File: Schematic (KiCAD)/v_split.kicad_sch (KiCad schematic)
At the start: 108 parts, among them P1 INVERT, P10 NAND_2, P11 NAND_2, P12,13,18,19,25,26 Reg 3 DFF-Reset, P14 INVERT, P15 T-FF Preload, P16 NAND_2, P17 NAND_2, P2 NOR_2, P20 INVERT, P21 T-FF Preload, P22 BUFFER, P23 NAND_2, P24 NAND_2, P28 BUFFER, P3 INVERT, P6 Reg 2 DFF-Reset N, P8 INVERT, P9 T-FF Preload, T1 INVERT, T10 INVERT, T12 T-FF Preload, T13 INVERT, T14 INVERT, T15 T-FF Preload, T16 INVERT, T17 INVERT, T18 T-FF Preload, T19 INVERT, T2 INVERT, T20 INVERT, T21 T-FF Preload, T22 INVERT, T23 INVERT, T24 T-FF Preload, T25 INVERT, T26 INVERT, T27 T-FF Preload, T28 INVERT, T29 INVERT, T3 NAND_2, T30 T-FF Preload, T31 INVERT, T4 JK-FF Reset, T5 BUFFER, T6 INVERT, T7 INVERT, T8 T-FF Preload, T9 INVERT, X1 INVERT, X2 NAND_2

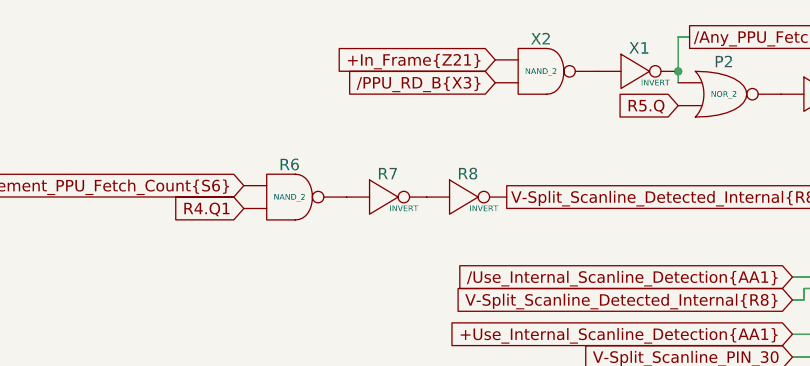
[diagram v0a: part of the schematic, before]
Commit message: - Started work on the pulse channels.  - Solved at least 2 of the red traces in the SVG.  - Finally realized that "Unknown 4to1" cells are actually just ordinary And-Or-Invert "AOI22" cells.
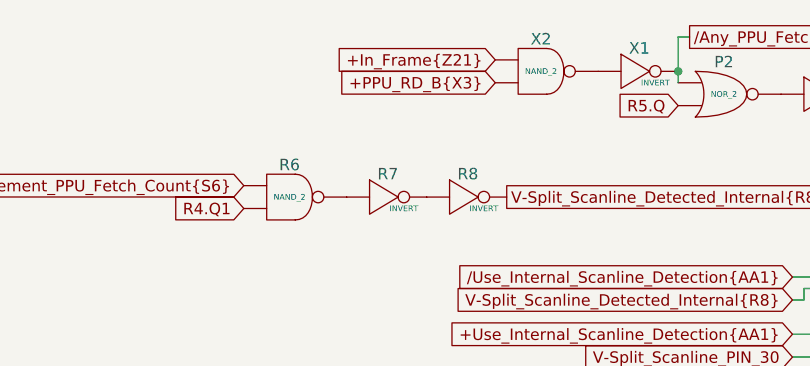
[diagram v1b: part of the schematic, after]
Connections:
- net /PPU_RD_B{X3} is gone; now on net +PPU_RD_B{X3}: X2. (X)
- net at V4. (X): now also V5. (X); no longer V6. (X)
- net at V9. (X): now also V11. (X); no longer V4. (X)
- net at R27. (/Q): now also R26. (X)
- net at R26. (X): now also R29. (X); no longer R27. (/Q)
- net at P9. (/Q): now also P8. (X); no longer P10. (X)
- net at T2. (X): now also T1. (X); no longer T3. (X)
- net at P28. (X): now also R26. (X); no longer P12,13,18,19,25,26. (Q2)
- net at T20. (X): now also T21. (/Q); no longer V27. (X)
- net at T21. (/Q): now also V28. (X), V29. (X); no longer T20. (X)
- net at R7. (X): now also R8. (X); no longer R6. (X)
- net at P21. (/Q): no longer P22. (X)
- net at T14. (X): now also T15. (/Q); no longer V19. (X)
- net at P1. (X): now also P2. (X); no longer S5. (X)
- net at T29. (X): now also V36. (X); no longer T30. (/Q)
- net at P15. (/Q): now also P20. (X), P21. (/Q); no longer P16. (X)
- net at BH28. (X): now also T4. (/Q); no longer BH29. (X)
- net at V11. (X): now also V10. (X); no longer V12. (X)
- net at T26. (X): now also T27. (/Q); no longer V33. (X)
- net at T27. (/Q): no longer T26. (X)
- net at T12. (/Q): now also T8. (/Q), T9. (X)
- net at T10. (X): now also V16. (X); no longer T12. (/Q)
- net at T30. (/Q): now also V37. (X), V38. (X); no longer T31. (X)
- net at T23. (X): now also V30. (X); no longer T24. (/Q)
- net at T15. (/Q): no longer T14. (X)
- net at BH32. (X): now also BH31. (X); no longer T4. (/Q)
- net at T7. (X): now also T8. (/Q); no longer V13. (X)
- net +PPU_RD_B{X3}: now reaches X2. (X)
- net +PPU_RD_B{X3}: no longer X1. (X)
- net at T18. (/Q): now also T17. (X)
- net at T17. (X): now also V22. (X); no longer T18. (/Q)
- new net: N1. (X), P6. (/Q1)
- new net: V4. (X), V6. (X)
- new net: V3. (X), V4. (X)
- new net: V4. (X), V9. (X)
- new net: R27. (/Q), R28. (X)
- new net: R27. (/Q), R29. (X)
- new net: P3. (X), R1. (X)
- new net: P10. (X), P9. (/Q)
- new net: P10. (X), P11. (X), P9. (/Q)
- new net: T2. (X), T3. (X)
- new net: T3. (X), T4. (/Q)
- new net: T18. (/Q), T19. (X), T21. (/Q)
- new net: T15. (/Q), T16. (X), T18. (/Q)
- new net: V6. (X), W2. (Q4)
- new net: P12,13,18,19,25,26. (Q2), P28. (X)
- new net: P12,13,18,19,25,26. (Q2), P17. (X)
- new net: P11. (X), P12,13,18,19,25,26. (Q2)
- new net: P12,13,18,19,25,26. (Q2), P24. (X)
- new net: P14. (X), P15. (/Q), P9. (/Q)
- new net: T20. (X), V27. (X)
- new net: R6. (X), R7. (X)
- new net: T27. (/Q), V34. (X), V35. (X)
- new net: V33. (X), V34. (X)
- new net: P21. (/Q), P22. (X)
- new net: V19. (X), V20. (X)
- new net: T14. (X), V19. (X)
- new net: V7. (X), V8. (/Q)
- new net: P1. (X), S5. (X)
- new net: V27. (X), V28. (X)
- new net: V3. (X), W2. (Q4)
- new net: T29. (X), T30. (/Q)
- new net: P15. (/Q), P16. (X), P17. (X)
- new net: P15. (/Q), P16. (X)
- new net: T18. (/Q), V23. (X), V26. (X)
- new net: V26. (X), W3,V24,V25,V41. (Q7)
- new net: V8. (/Q), V9. (X)
- new net: V35. (X), W3,V24,V25,V41. (Q7)
- new net: BH28. (X), BH29. (X)
- new net: V11. (X), V12. (X)
- new net: V12. (X), W2. (Q4)
- new net: P21. (/Q), P23. (X)
- new net: P21. (/Q), P23. (X), P24. (X)
- new net: T24. (/Q), T25. (X), T27. (/Q)
- new net: T26. (X), V33. (X)
- new net: T15. (/Q), V20. (X), V21. (X)
- new net: R4. (Q1), S4. (X)
- new net: R4. (Q1), S3. (X)
- new net: T12. (/Q), V17. (X), V18. (X)
- new net: T12. (/Q), T13. (X), T15. (/Q)
- new net: T10. (X), T12. (/Q)
- new net: V22. (X), V23. (X)
- new net: V18. (X), W3,V24,V25,V41. (Q7)
- new net: T30. (/Q), T31. (X)
- new net: T23. (X), T24. (/Q)
- new net: T21. (/Q), T22. (X), T24. (/Q)
- new net: BH29. (X), BH30. (X)
- new net: BH32. (X), T4. (/Q)
- new net: T27. (/Q), T28. (X), T30. (/Q)
- new net: V16. (X), V17. (X)
- new net: T7. (X), V13. (X)
- new net: V13. (X), V14. (X)
- new net: V5. (X), W2. (Q4)
- new net: V36. (X), V37. (X)
- new net: T24. (/Q), V31. (X), V32. (X)
- new net: V32. (X), W3,V24,V25,V41. (Q7)
- new net: V29. (X), W3,V24,V25,V41. (Q7)
- new net: X1. (X), X2. (X)
- new net: T6. (X), V11. (X)
- new net: V30. (X), V31. (X)
- new net: V38. (X), W3,V24,V25,V41. (Q7)
- new net: T8. (/Q), V14. (X), V15. (X)
- new net: V2. (X), W2. (Q4)
- new net: V21. (X), W3,V24,V25,V41. (Q7)
- new net: V15. (X), W3,V24,V25,V41. (Q7)
- new net: V10. (X), W2. (Q4)
- now unconnected: P21. (/Q), P21. (/Q), P21. (/Q), T15. (/Q), T15. (/Q), T15. (/Q), T24. (/Q), T24. (/Q), T24. (/Q), T27. (/Q), T27. (/Q), T27. (/Q)
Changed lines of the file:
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@@
 		)
 	)
-	(global_label "{slash}PPU_RD_B{X3}"
+	(global_label "+PPU_RD_B{X3}"
 		(shape input)
 		(at 264.16 24.13 180)
@@
 		)
 		(property "Intersheetrefs" "${INTERSHEET_REFS}"
-			(at 246.1162 24.13 0)
+			(at 245.8743 24.13 0)
 			(effects
 				(font

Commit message: - Pulse DAC logic is now complete.  - The 4-bit adders are verified correct using Excel.    - This revealed 1 tracing error and also 3 XNOR gates that are actually XOR in this case.  - Now including a PDF version of the schematic.
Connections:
- net at V4. (X): now also V5. (X); no longer V6. (X)
- net at V9. (X): now also V11. (X); no longer V4. (X)
- net at R27. (/Q): now also R26. (X)
- net at R26. (X): now also R29. (X); no longer R27. (/Q)
- net at P9. (/Q): now also P8. (X); no longer P10. (X)
- net at T2. (X): now also T1. (X); no longer T3. (X)
- net at P28. (X): now also R26. (X); no longer P12,13,18,19,25,26. (Q2)
- net at T20. (X): now also T21. (/Q); no longer V27. (X)
- net at T21. (/Q): now also V28. (X), V29. (X); no longer T20. (X)
- net at R7. (X): now also R8. (X); no longer R6. (X)
- net at P21. (/Q): no longer P22. (X)
- net at T14. (X): now also T15. (/Q); no longer V19. (X)
- net at P1. (X): now also P2. (X); no longer S5. (X)
- net at T29. (X): now also V36. (X); no longer T30. (/Q)
- net at P15. (/Q): now also P20. (X), P21. (/Q); no longer P16. (X)
- net at BH28. (X): now also T4. (/Q); no longer BH29. (X)
- net at V11. (X): now also V10. (X); no longer V12. (X)
- net at T26. (X): now also T27. (/Q); no longer V33. (X)
- net at T27. (/Q): no longer T26. (X)
- net at T12. (/Q): now also T8. (/Q), T9. (X)
- net at T10. (X): now also V16. (X); no longer T12. (/Q)
- net at T30. (/Q): now also V37. (X), V38. (X); no longer T31. (X)
- net at T23. (X): now also V30. (X); no longer T24. (/Q)
- net at T15. (/Q): no longer T14. (X)
- net at BH32. (X): now also BH31. (X); no longer T4. (/Q)
- net at T7. (X): now also T8. (/Q); no longer V13. (X)
- net at T18. (/Q): now also T17. (X)
- net at T17. (X): now also V22. (X); no longer T18. (/Q)
- new net: N1. (X), P6. (/Q1)
- new net: V4. (X), V6. (X)
- new net: V3. (X), V4. (X)
- new net: V4. (X), V9. (X)
- new net: R27. (/Q), R28. (X)
- new net: R27. (/Q), R29. (X)
- new net: P3. (X), R1. (X)
- new net: P10. (X), P9. (/Q)
- new net: P10. (X), P11. (X), P9. (/Q)
- new net: T2. (X), T3. (X)
- new net: T3. (X), T4. (/Q)
- new net: T18. (/Q), T19. (X), T21. (/Q)
- new net: T15. (/Q), T16. (X), T18. (/Q)
- new net: V6. (X), W2. (Q4)
- new net: P12,13,18,19,25,26. (Q2), P28. (X)
- new net: P12,13,18,19,25,26. (Q2), P17. (X)
- new net: P11. (X), P12,13,18,19,25,26. (Q2)
- new net: P12,13,18,19,25,26. (Q2), P24. (X)
- new net: P14. (X), P15. (/Q), P9. (/Q)
- new net: T20. (X), V27. (X)
- new net: R6. (X), R7. (X)
- new net: T27. (/Q), V34. (X), V35. (X)
- new net: V33. (X), V34. (X)
- new net: P21. (/Q), P22. (X)
- new net: V19. (X), V20. (X)
- new net: T14. (X), V19. (X)
- new net: V7. (X), V8. (/Q)
- new net: P1. (X), S5. (X)
- new net: V27. (X), V28. (X)
- new net: V3. (X), W2. (Q4)
- new net: T29. (X), T30. (/Q)
- new net: P15. (/Q), P16. (X), P17. (X)
- new net: P15. (/Q), P16. (X)
- new net: T18. (/Q), V23. (X), V26. (X)
- new net: V26. (X), W3,V24,V25,V41. (Q7)
- new net: V8. (/Q), V9. (X)
- new net: V35. (X), W3,V24,V25,V41. (Q7)
- new net: BH28. (X), BH29. (X)
- new net: V11. (X), V12. (X)
- new net: V12. (X), W2. (Q4)
- new net: P21. (/Q), P23. (X)
- new net: P21. (/Q), P23. (X), P24. (X)
- new net: T24. (/Q), T25. (X), T27. (/Q)
- new net: T26. (X), V33. (X)
- new net: T15. (/Q), V20. (X), V21. (X)
- new net: R4. (Q1), S4. (X)
- new net: R4. (Q1), S3. (X)
- new net: T12. (/Q), V17. (X), V18. (X)
- new net: T12. (/Q), T13. (X), T15. (/Q)
- new net: T10. (X), T12. (/Q)
- new net: V22. (X), V23. (X)
- new net: V18. (X), W3,V24,V25,V41. (Q7)
- new net: T30. (/Q), T31. (X)
- new net: T23. (X), T24. (/Q)
- new net: T21. (/Q), T22. (X), T24. (/Q)
- new net: BH29. (X), BH30. (X)
- new net: BH32. (X), T4. (/Q)
- new net: T27. (/Q), T28. (X), T30. (/Q)
- new net: V16. (X), V17. (X)
- new net: T7. (X), V13. (X)
- new net: V13. (X), V14. (X)
- new net: V5. (X), W2. (Q4)
- new net: V36. (X), V37. (X)
- new net: T24. (/Q), V31. (X), V32. (X)
- new net: V32. (X), W3,V24,V25,V41. (Q7)
- new net: V29. (X), W3,V24,V25,V41. (Q7)
- new net: X1. (X), X2. (X)
- new net: T6. (X), V11. (X)
- new net: V30. (X), V31. (X)
- new net: V38. (X), W3,V24,V25,V41. (Q7)
- new net: T8. (/Q), V14. (X), V15. (X)
- new net: V2. (X), W2. (Q4)
- new net: V21. (X), W3,V24,V25,V41. (Q7)
- new net: V15. (X), W3,V24,V25,V41. (Q7)
- new net: V10. (X), W2. (Q4)
- now unconnected: P21. (/Q), P21. (/Q), P21. (/Q), T15. (/Q), T15. (/Q), T15. (/Q), T24. (/Q), T24. (/Q), T24. (/Q), T27. (/Q), T27. (/Q), T27. (/Q)

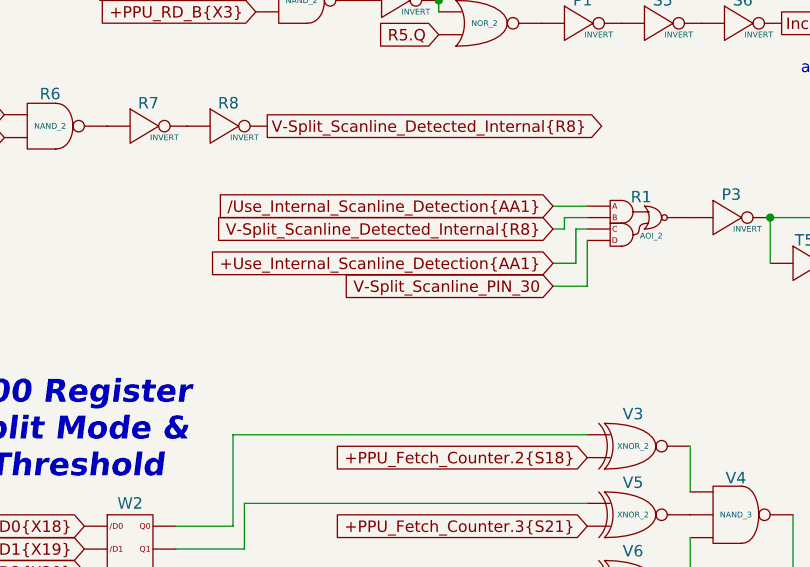
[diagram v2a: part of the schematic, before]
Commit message: - All cells in the left and center areas have now been added into the schematics.  - Changed naming of the PDF files; I was accidentally writing over furrtek's original with my new PDF.
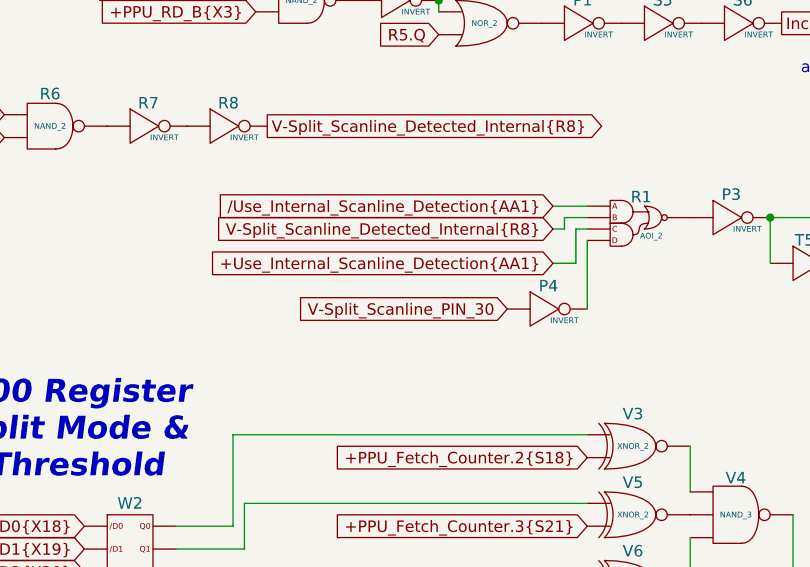
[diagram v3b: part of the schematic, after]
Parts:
- added P4: INVERT, symbol MMC5:INVERT
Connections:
- net V-Split_Scanline_PIN_30: now also P4. (X); no longer R1. (X)
- net at V4. (X): now also V5. (X); no longer V6. (X)
- net at V9. (X): now also V11. (X); no longer V4. (X)
- net at R27. (/Q): now also R26. (X)
- net at R26. (X): now also R29. (X); no longer R27. (/Q)
- net at P9. (/Q): now also P8. (X); no longer P10. (X)
- net at T2. (X): now also T1. (X); no longer T3. (X)
- net at P28. (X): now also R26. (X); no longer P12,13,18,19,25,26. (Q2)
- net at T20. (X): now also T21. (/Q); no longer V27. (X)
- net at T21. (/Q): now also V28. (X), V29. (X); no longer T20. (X)
- net at R7. (X): now also R8. (X); no longer R6. (X)
- net at P21. (/Q): no longer P22. (X)
- net at T14. (X): now also T15. (/Q); no longer V19. (X)
- net at P1. (X): now also P2. (X); no longer S5. (X)
- net at T29. (X): now also V36. (X); no longer T30. (/Q)
- net at P15. (/Q): now also P20. (X), P21. (/Q); no longer P16. (X)
- net at BH28. (X): now also T4. (/Q); no longer BH29. (X)
- net at V11. (X): now also V10. (X); no longer V12. (X)
- net at T26. (X): now also T27. (/Q); no longer V33. (X)
- net at T27. (/Q): no longer T26. (X)
- net at T12. (/Q): now also T8. (/Q), T9. (X)
- net at T10. (X): now also V16. (X); no longer T12. (/Q)
- net at T30. (/Q): now also V37. (X), V38. (X); no longer T31. (X)
- net at T23. (X): now also V30. (X); no longer T24. (/Q)
- net at T15. (/Q): no longer T14. (X)
- net at BH32. (X): now also BH31. (X); no longer T4. (/Q)
- net at T7. (X): now also T8. (/Q); no longer V13. (X)
- net at T18. (/Q): now also T17. (X)
- net at T17. (X): now also V22. (X); no longer T18. (/Q)
- new net: N1. (X), P6. (/Q1)
- new net: V4. (X), V6. (X)
- new net: V3. (X), V4. (X)
- new net: V4. (X), V9. (X)
- new net: R27. (/Q), R28. (X)
- new net: R27. (/Q), R29. (X)
- new net: P4. (X), R1. (X)
- new net: P3. (X), R1. (X)
- new net: P10. (X), P9. (/Q)
- new net: P10. (X), P11. (X), P9. (/Q)
- new net: T2. (X), T3. (X)
- new net: T3. (X), T4. (/Q)
- new net: T18. (/Q), T19. (X), T21. (/Q)
- new net: T15. (/Q), T16. (X), T18. (/Q)
- new net: V6. (X), W2. (Q4)
- new net: P12,13,18,19,25,26. (Q2), P28. (X)
- new net: P12,13,18,19,25,26. (Q2), P17. (X)
- new net: P11. (X), P12,13,18,19,25,26. (Q2)
- new net: P12,13,18,19,25,26. (Q2), P24. (X)
- new net: P14. (X), P15. (/Q), P9. (/Q)
- new net: T20. (X), V27. (X)
- new net: R6. (X), R7. (X)
- new net: T27. (/Q), V34. (X), V35. (X)
- new net: V33. (X), V34. (X)
- new net: P21. (/Q), P22. (X)
- new net: V19. (X), V20. (X)
- new net: T14. (X), V19. (X)
- new net: V7. (X), V8. (/Q)
- new net: P1. (X), S5. (X)
- new net: V27. (X), V28. (X)
- new net: V3. (X), W2. (Q4)
- new net: T29. (X), T30. (/Q)
- new net: P15. (/Q), P16. (X), P17. (X)
- new net: P15. (/Q), P16. (X)
- new net: T18. (/Q), V23. (X), V26. (X)
- new net: V26. (X), W3,V24,V25,V41. (Q7)
- new net: V8. (/Q), V9. (X)
- new net: V35. (X), W3,V24,V25,V41. (Q7)
- new net: BH28. (X), BH29. (X)
- new net: V11. (X), V12. (X)
- new net: V12. (X), W2. (Q4)
- new net: P21. (/Q), P23. (X)
- new net: P21. (/Q), P23. (X), P24. (X)
- new net: T24. (/Q), T25. (X), T27. (/Q)
- new net: T26. (X), V33. (X)
- new net: T15. (/Q), V20. (X), V21. (X)
- new net: R4. (Q1), S4. (X)
- new net: R4. (Q1), S3. (X)
- new net: T12. (/Q), V17. (X), V18. (X)
- new net: T12. (/Q), T13. (X), T15. (/Q)
- new net: T10. (X), T12. (/Q)
- new net: V22. (X), V23. (X)
- new net: V18. (X), W3,V24,V25,V41. (Q7)
- new net: T30. (/Q), T31. (X)
- new net: T23. (X), T24. (/Q)
- new net: T21. (/Q), T22. (X), T24. (/Q)
- new net: BH29. (X), BH30. (X)
- new net: BH32. (X), T4. (/Q)
- new net: T27. (/Q), T28. (X), T30. (/Q)
- new net: V16. (X), V17. (X)
- new net: T7. (X), V13. (X)
- new net: V13. (X), V14. (X)
- new net: V5. (X), W2. (Q4)
- new net: V36. (X), V37. (X)
- new net: T24. (/Q), V31. (X), V32. (X)
- new net: V32. (X), W3,V24,V25,V41. (Q7)
- new net: V29. (X), W3,V24,V25,V41. (Q7)
- new net: X1. (X), X2. (X)
- new net: T6. (X), V11. (X)
- new net: V30. (X), V31. (X)
- new net: V38. (X), W3,V24,V25,V41. (Q7)
- new net: T8. (/Q), V14. (X), V15. (X)
- new net: V2. (X), W2. (Q4)
- new net: V21. (X), W3,V24,V25,V41. (Q7)
- new net: V15. (X), W3,V24,V25,V41. (Q7)
- new net: V10. (X), W2. (Q4)
- now unconnected: P21. (/Q), P21. (/Q), P21. (/Q), T15. (/Q), T15. (/Q), T15. (/Q), T24. (/Q), T24. (/Q), T24. (/Q), T27. (/Q), T27. (/Q), T27. (/Q)
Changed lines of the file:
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@@
 	(wire
 		(pts
-			(xy 297.18 54.61) (xy 300.99 54.61)
-		)
-		(stroke
-			(width 0)
-			(type default)
-		)
-	)
-	(wire
-		(pts
 			(xy 176.53 191.77) (xy 176.53 198.12)
 		)
@@
 	(wire
 		(pts
-			(xy 300.99 54.61) (xy 300.99 49.53)
-		)
-		(stroke
-			(width 0)
-			(type default)
-		)
-	)
-	(wire
-		(pts
 			(xy 140.97 85.09) (xy 142.24 85.09)
 		)
@@
 	(wire
 		(pts
+			(xy 300.99 49.53) (xy 300.99 57.15)
+		)
+		(stroke
+			(width 0)
+			(type default)
+		)
+	)
+	(wire
+		(pts
 			(xy 93.98 102.87) (xy 105.41 102.87)
 		)
@@
 	(global_label "V-Split_Scanline_PIN_30"
 		(shape input)
-		(at 297.18 54.61 180)
+		(at 292.1 57.15 180)
 		(fields_autoplaced yes)
 		(effects
@@
 		)
 		(property "Intersheetrefs" "${INTERSHEET_REFS}"
-			(at 270.5488 54.61 0)
+			(at 265.4688 57.15 0)
 			(effects
 				(font
@@
 					(unit 1)
 				)
+			)
+		)
+	)
+	(symbol
+		(lib_name "INVERT_33")
+		(lib_id "MMC5:INVERT")
+		(at 297.18 57.15 0)
+		(unit 1)
+		(exclude_from_sim no)
+		(in_bom yes)
+		(on_board yes)
+		(dnp no)
+		(fields_autoplaced yes)
+		(property "Reference" "P4"
+			(at 296.672 53.848 0)
+			(do_not_autoplace yes)
+			(effects
+				(font
+					(size 1.27 1.27)
+				)
+				(justify top)
+			)
+		)
+		(property "Value" "INVERT"
+			(at 298.45 58.42 0)
+			(do_not_autoplace yes)
+			(effects
+				(font
+					(size 0.635 0.635)
+				)
+			)
+		)
+		(property "Footprint" ""
+			(at 297.18 57.15 0)
+			(effects
+				(font
+					(size 1.27 1.27)
+				)
+				(hide yes)
+			)
+		)
+		(property "Datasheet" ""
+			(at 297.18 57.15 0)
+			(effects
+				(font
+					(size 1.27 1.27)
+				)
+				(hide yes)
+			)
+		)
+		(property "Description" ""
+			(at 297.18 57.15 0)
+			(effects
+				(font
+					(size 1.27 1.27)
+				)
+				(hide yes)
+			)
+		)
+		(pin ""
+		)
+		(pin ""
+		)
+		(instances
+			(project "MMC5"
+				(path "/46093bf6-f83e-4237-9ece-7350a682aff0/f99076a8-83c5-44a3-a289-c8e87f9c162a"
+					(reference "P4")
+					(unit 1)
+				)
